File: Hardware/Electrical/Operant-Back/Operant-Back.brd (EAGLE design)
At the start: 33.6 x 45.4 mm, 9 parts

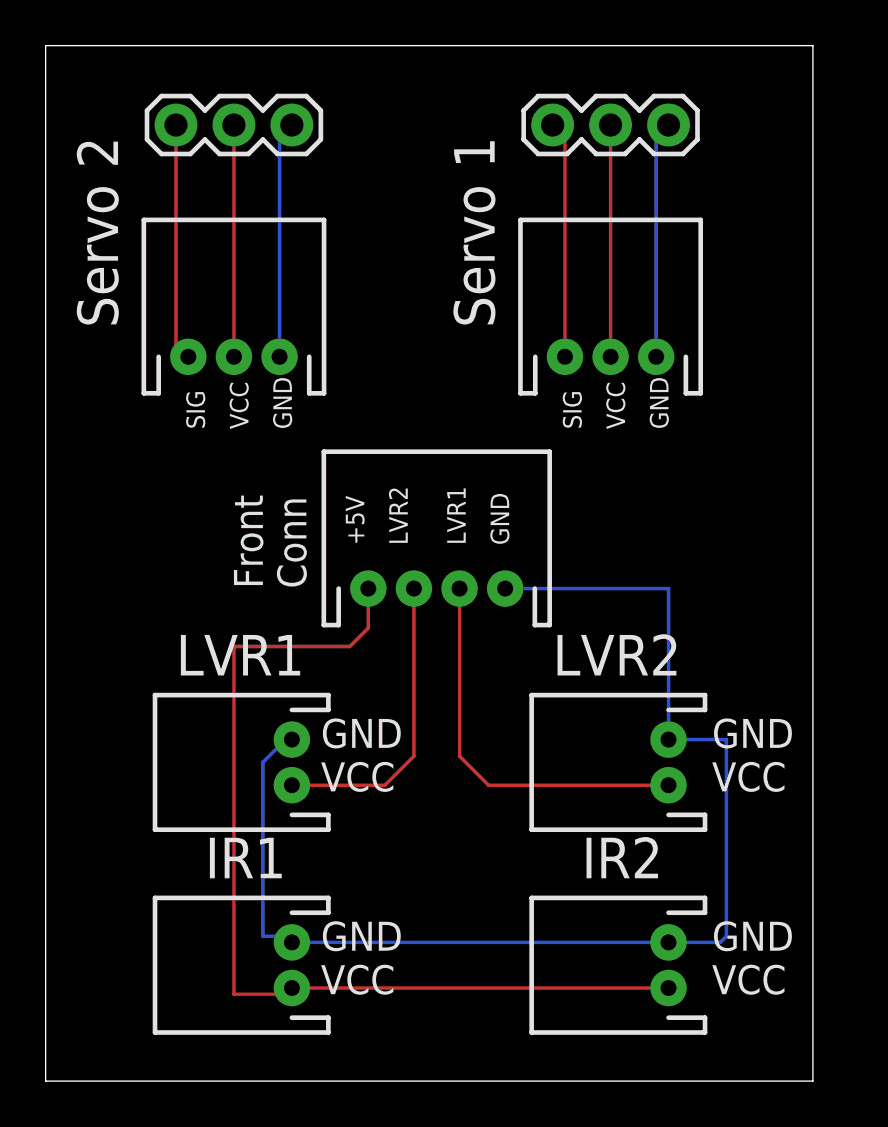
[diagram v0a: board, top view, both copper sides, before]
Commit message: Added dims
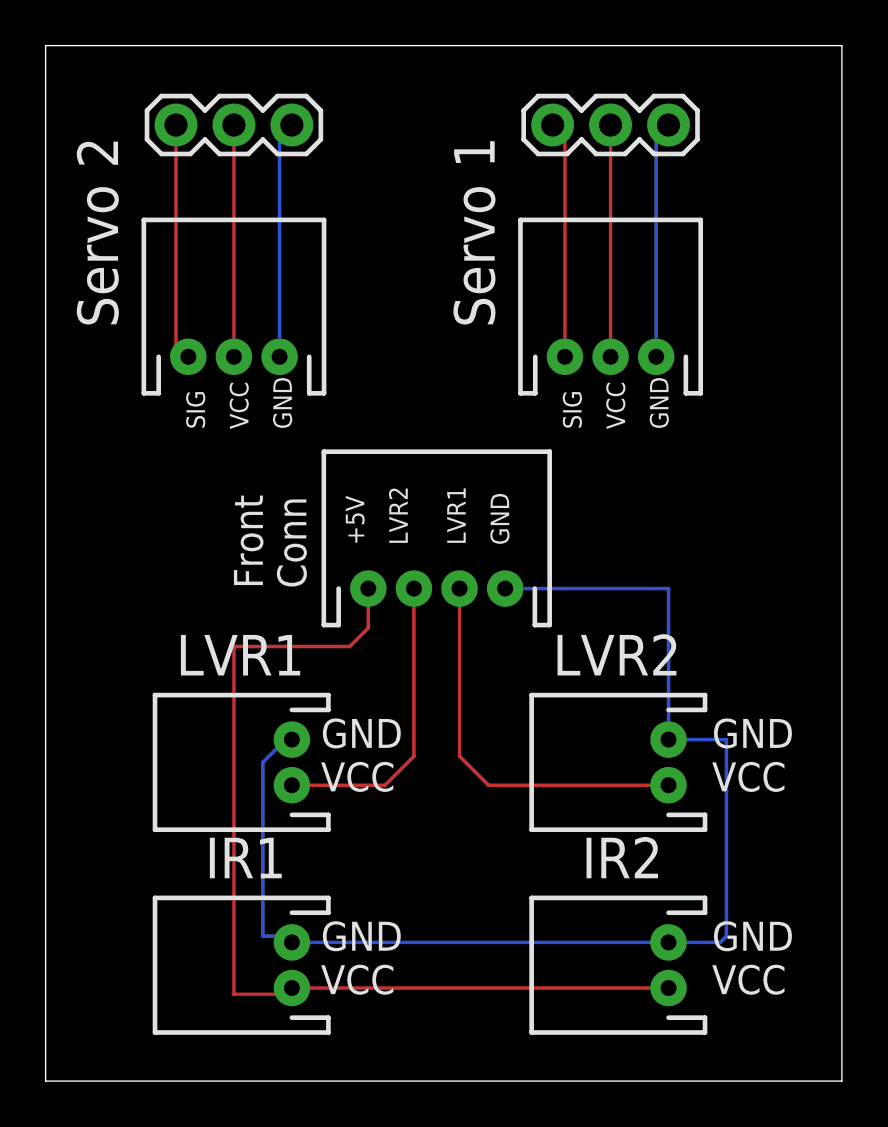
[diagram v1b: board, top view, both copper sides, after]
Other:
- board size 33.6 x 45.4 mm -> 34.9 x 45.4 mm
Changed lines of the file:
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@@
 <setting verticaltext="up"/>
 </settings>
-<grid distance="25" unitdist="mil" unit="mil" style="lines" multiple="1" display="yes" altdistance="5" altunitdist="mil" altunit="mil"/>
+<grid distance="50" unitdist="mil" unit="mil" style="lines" multiple="1" display="yes" altdistance="5" altunitdist="mil" altunit="mil"/>
 <layers>
 <layer number="1" name="Top" color="4" fill="1" visible="yes" active="yes"/>
@@
 <board>
 <plain>
-<wire x1="0" y1="0" x2="33.635" y2="0" width="0" layer="20"/>
-<wire x1="33.635" y1="0" x2="33.635" y2="45.39" width="0" layer="20"/>
-<wire x1="33.635" y1="45.39" x2="0" y2="45.39" width="0" layer="20"/>
+<wire x1="0" y1="0" x2="34.905" y2="0" width="0" layer="20"/>
+<wire x1="34.905" y1="0" x2="34.905" y2="45.39" width="0" layer="20"/>
+<wire x1="34.905" y1="45.39" x2="0" y2="45.39" width="0" layer="20"/>
 <wire x1="0" y1="45.39" x2="0" y2="0" width="0" layer="20"/>
 <text x="3.175" y="33.02" size="1.778" layer="21" rot="R90">Servo 2</text>
@@
 <text x="6.35" y="38.1" size="0.8128" layer="22" rot="R90">SIG</text>
 <text x="22.86" y="38.1" size="0.8128" layer="22" rot="R90">SIG</text>
+<dimension x1="0" y1="45.39" x2="0" y2="0" x3="-6.35" y3="22.695" textsize="0.8128" layer="20"/>
+<dimension x1="0" y1="0" x2="34.905" y2="0" x3="17.4525" y3="-2.54" textsize="0.8128" layer="20"/>
 </plain>
 <attributes>
